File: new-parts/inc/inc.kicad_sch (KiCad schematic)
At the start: 20 parts, among them J1 BHR-10-VUA, J2 BHR-10-VUA, J3 Conn_01x01, J4 Conn_01x01, K1 J104D2C12VDC.15S, K2 J104D2C12VDC.15S, K3 J104D2C12VDC.15S, K4 J104D2C12VDC.15S, K5 J104D2C12VDC.15S, K6 J104D2C12VDC.15S, K7 J104D2C12VDC.15S, K8 J104D2C12VDC.15S

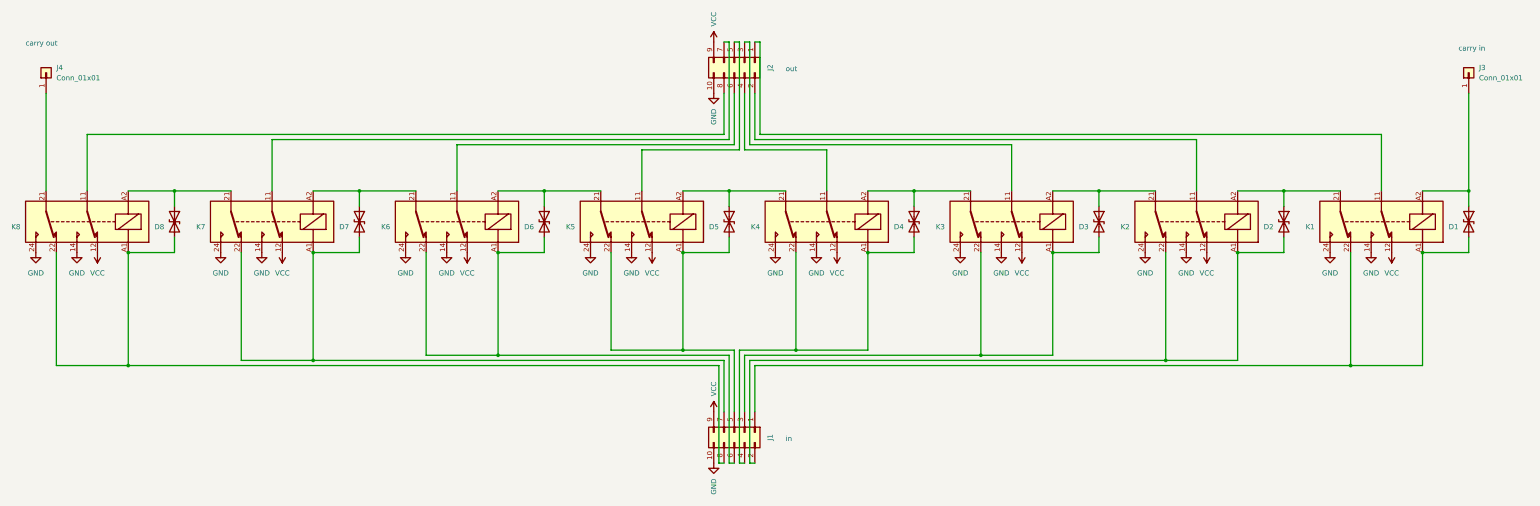
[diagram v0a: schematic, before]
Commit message: inc: Fix inverted output.
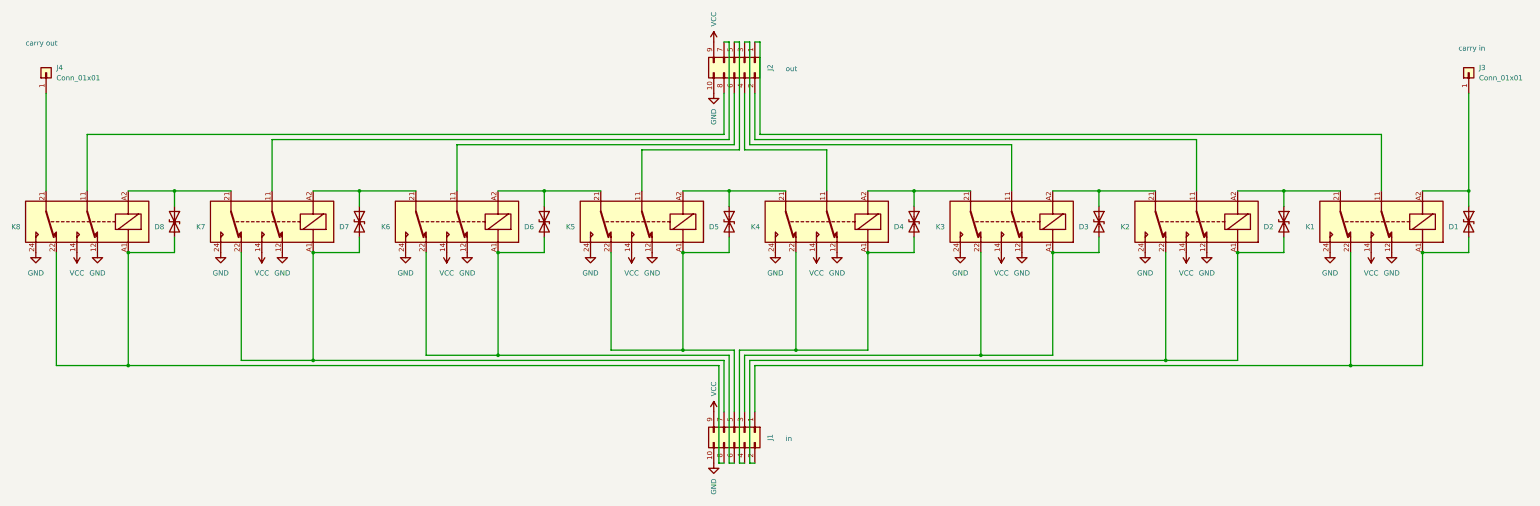
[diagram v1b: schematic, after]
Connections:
- net GND: now also K1.12, K2.12, K3.12, K4.12, K5.12, K6.12, K7.12, K8.12; no longer K1.14, K2.14, K3.14, K4.14, K5.14, K6.14, K7.14, K8.14
- net VCC: now also K1.14, K2.14, K3.14, K4.14, K5.14, K6.14, K7.14, K8.14; no longer K1.12, K2.12, K3.12, K4.12, K5.12, K6.12, K7.12, K8.12

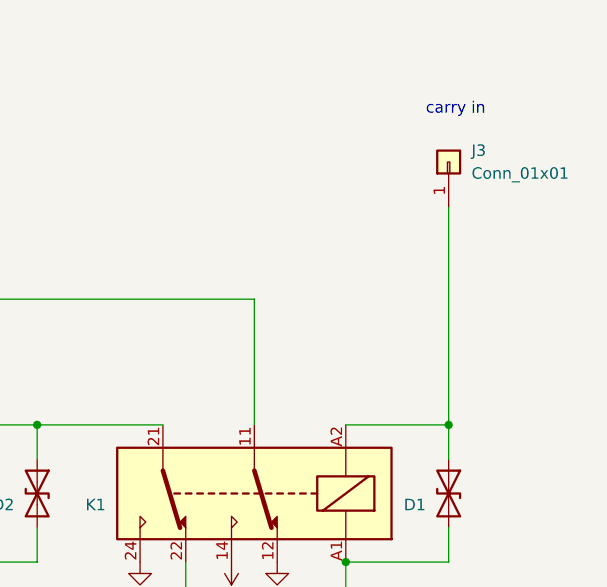
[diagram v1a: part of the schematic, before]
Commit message: inc: Add solder jumper for stanalone operation (carry in = 1).
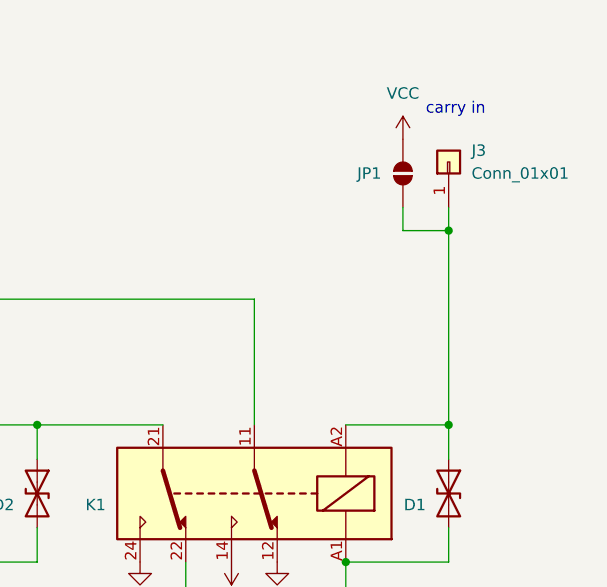
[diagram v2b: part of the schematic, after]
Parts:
- added JP1: SolderJumper_2_Open, Jumper:SolderJumper-2_P1.3mm_Open_TrianglePad1.0x1.5mm, symbol Jumper:SolderJumper_2_Open
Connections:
- net VCC: now also JP1.2 (B)
- net at D1.1 (A1), J3.1 (Pin_1), K1.A2: now also JP1.1 (A)
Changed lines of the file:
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@@
+	)
+	(junction
+		(at 388.62 82.55)
+		(diameter 0)
+		(color 0 0 0 0)
 	)
 	(junction
@@
 	(wire
 		(pts
+			(xy 383.54 80.01) (xy 383.54 82.55)
+		)
+		(stroke
+			(width 0)
+			(type default)
+		)
+	)
+	(wire
+		(pts
 			(xy 210.82 146.05) (xy 313.69 146.05)
 		)
@@
 	(wire
 		(pts
-			(xy 388.62 80.01) (xy 388.62 104.14)
+			(xy 388.62 80.01) (xy 388.62 82.55)
 		)
 		(stroke
@@
 	(wire
 		(pts
+			(xy 388.62 82.55) (xy 388.62 104.14)
+		)
+		(stroke
+			(width 0)
+			(type default)
+		)
+	)
+	(wire
+		(pts
 			(xy 205.74 144.78) (xy 148.59 144.78)
 		)
@@
 		(pts
 			(xy 68.58 119.38) (xy 57.15 119.38)
+		)
+		(stroke
+			(width 0)
+			(type default)
+		)
+	)
+	(wire
+		(pts
+			(xy 383.54 82.55) (xy 388.62 82.55)
 		)
 		(stroke
@@
 	)
 	(symbol
+		(lib_id "Jumper:SolderJumper_2_Open")
+		(at 383.54 76.2 90)
+		(unit 1)
+		(exclude_from_sim yes)
+		(in_bom no)
+		(on_board yes)
+		(dnp no)
+		(property "Reference" "JP1"
+			(at 378.46 76.2 90)
+			(effects
+				(font
+					(size 1.27 1.27)
+				)
+				(justify right)
+			)
+		)
+		(property "Value" "SolderJumper_2_Open"
+			(at 386.08 77.4699 90)
+			(effects
+				(font
+					(size 1.27 1.27)
+				)
+				(justify right)
+				(hide yes)
+			)
+		)
+		(property "Footprint" "Jumper:SolderJumper-2_P1.3mm_Open_TrianglePad1.0x1.5mm"
+			(at 383.54 76.2 0)
+			(effects
+				(font
+					(size 1.27 1.27)
+				)
+				(hide yes)
+			)
+		)
+		(property "Datasheet" "~"
+			(at 383.54 76.2 0)
+			(effects
+				(font
+					(size 1.27 1.27)
+				)
+				(hide yes)
+			)
+		)
+		(property "Description" "Solder Jumper, 2-pole, open"
+			(at 383.54 76.2 0)
+			(effects
+				(font
+					(size 1.27 1.27)
+				)
+				(hide yes)
+			)
+		)
+		(pin "1"
+		)
+		(pin "2"
+		)
+		(instances
+			(project "inc"
+				(path "/8e7358e7-c3ef-4f3e-9154-e7eba01c544e"
+					(reference "JP1")
+					(unit 1)
+				)
+			)
+		)
+	)
+	(symbol
 		(lib_id "Connector_Generic:Conn_02x05_Odd_Even")
 		(at 207.01 72.39 270)
@@
 					(unit 1)
 				)
+			)
+		)
+	)
+	(symbol
+		(lib_id "power:VCC")
+		(at 383.54 72.39 0)
+		(unit 1)
+		(exclude_from_sim no)
+		(in_bom yes)
+		(on_board yes)
+		(dnp no)
+		(fields_autoplaced yes)
+		(property "Reference" "#PWR027"
+			(at 383.54 76.2 0)
+			(effects
+				(font
+					(size 1.27 1.27)
+				)
+				(hide yes)
+			)
+		)
+		(property "Value" "VCC"
+			(at 383.54 67.31 0)
+			(effects
+				(font
+					(size 1.27 1.27)
+				)
+			)
+		)
+		(property "Footprint" ""
+			(at 383.54 72.39 0)
+			(effects
+				(font
+					(size 1.27 1.27)
+				)
+				(hide yes)
+			)
+		)
+		(property "Datasheet" ""
+			(at 383.54 72.39 0)
+			(effects
+				(font
+					(size 1.27 1.27)
+				)
+				(hide yes)
+			)
+		)
+		(property "Description" ""
+			(at 383.54 72.39 0)
+			(effects
+				(font
+					(size 1.27 1.27)
+				)
+				(hide yes)
+			)
+		)
+		(pin "1"
+		)
+		(instances
+			(project "inc"
+				(path "/8e7358e7-c3ef-4f3e-9154-e7eba01c544e"
+					(reference "#PWR027")
+					(unit 1)
+				)
